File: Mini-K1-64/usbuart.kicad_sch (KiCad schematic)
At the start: 12 parts, among them P1 USB_C_Plug_USB2.0, U1 CH343G, U3 AMS1117-3.3

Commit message: Format PCB
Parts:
- renumbered C8 to C1, C12 to C10, C9 to C7, JP3 to JP2, JP2 to JP3, R9 to R10, R10 to R12
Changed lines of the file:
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@@
 		(dnp no)
 		(fields_autoplaced yes)
-		(property "Reference" "JP2"
+		(property "Reference" "JP3"
 			(at 113.03 135.8901 90)
 			(effects
@@
 			(project "Mini-K1-64"
 				(path "/1a7e0d91-a6c0-4b42-a7c6-42574ab26c7c/391bf1b4-7921-4efb-b6a2-50abc6bbaaa6"
-					(reference "JP2")
+					(reference "JP3")
 					(unit 1)
 				)
@@
 		(dnp no)
 		(fields_autoplaced yes)
-		(property "Reference" "C8"
+		(property "Reference" "C1"
 			(at 180.34 123.1899 0)
 			(effects
@@
 			(project "Mini-K1-64"
 				(path "/1a7e0d91-a6c0-4b42-a7c6-42574ab26c7c/391bf1b4-7921-4efb-b6a2-50abc6bbaaa6"
-					(reference "C8")
+					(reference "C1")
 					(unit 1)
 				)
@@
 		(on_board yes)
 		(dnp yes)
-		(property "Reference" "JP3"
+		(property "Reference" "JP2"
 			(at 100.33 135.8901 90)
 			(effects
@@
 			(project "Mini-K1-64"
 				(path "/1a7e0d91-a6c0-4b42-a7c6-42574ab26c7c/391bf1b4-7921-4efb-b6a2-50abc6bbaaa6"
-					(reference "JP3")
+					(reference "JP2")
 					(unit 1)
 				)
@@
 		(dnp no)
 		(fields_autoplaced yes)
-		(property "Reference" "R9"
+		(property "Reference" "R10"
 			(at 171.45 111.7599 0)
 			(effects
@@
 			(project "Mini-K1-64"
 				(path "/1a7e0d91-a6c0-4b42-a7c6-42574ab26c7c/391bf1b4-7921-4efb-b6a2-50abc6bbaaa6"
-					(reference "R9")
+					(reference "R10")
 					(unit 1)
 				)
@@
 		(dnp no)
 		(fields_autoplaced yes)
-		(property "Reference" "R10"
+		(property "Reference" "R12"
 			(at 125.73 111.7599 0)
 			(effects
@@
 			(project "Mini-K1-64"
 				(path "/1a7e0d91-a6c0-4b42-a7c6-42574ab26c7c/391bf1b4-7921-4efb-b6a2-50abc6bbaaa6"
-					(reference "R10")
+					(reference "R12")
 					(unit 1)
 				)
@@
 		(dnp no)
 		(fields_autoplaced yes)
-		(property "Reference" "C9"
+		(property "Reference" "C7"
 			(at 167.64 123.1899 0)
 			(effects
@@
 			(project "Mini-K1-64"
 				(path "/1a7e0d91-a6c0-4b42-a7c6-42574ab26c7c/391bf1b4-7921-4efb-b6a2-50abc6bbaaa6"
-					(reference "C9")
+					(reference "C7")
 					(unit 1)
 				)
@@
 		(on_board yes)
 		(dnp no)
-		(property "Reference" "C12"
+		(property "Reference" "C10"
 			(at 135.89 123.1899 0)
 			(effects
@@
 			(project "Mini-K1-64"
 				(path "/1a7e0d91-a6c0-4b42-a7c6-42574ab26c7c/391bf1b4-7921-4efb-b6a2-50abc6bbaaa6"
-					(reference "C12")
-					(unit 1)
-				)
+					(reference "C10")
+					(unit 1)
+				)

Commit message: Step Update
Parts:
- removed P1: USB_C_Plug_USB2.0, Connector_USB:USB_C_Receptacle_GCT_USB4105-xx-A_16P_TopMnt_Horizontal, symbol Connector:USB_C_Plug_USB2.0
- removed U1: CH343G, Package_SO:SOIC-16_3.9x9.9mm_P1.27mm, symbol Interface_USB:CH343G
- added J6: USB_C_Receptacle_USB2.0_14P, Connector_USB:USB_C_Receptacle_GCT_USB4105-xx-A_16P_TopMnt_Horizontal, symbol Connector:USB_C_Receptacle_USB2.0_14P
- added R16: 5.1K, Resistor_SMD:R_0805_2012Metric, symbol Device:R
- added U1: CH340N, Package_SO:SOP-8_3.9x4.9mm_P1.27mm, symbol Interface_USB:CH340N
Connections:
- net OGND: now also J6.A1 (GND), J6.A12 (GND), J6.B1 (GND), J6.B12 (GND), J6.S1 (SHIELD), R16.2, U1.3 (GND)
- net UART_RX: now also U1.7 (RXD)
- net UART_TX: now also U1.6 (TXD)
- net UD+: now also J6.A6 (D+), J6.B6 (D+), U1.1 (UD+)
- net UD-: now also J6.A7 (D-), J6.B7 (D-), U1.2 (UD-)
- net VBUS: now also J6.A4 (VBUS), J6.A9 (VBUS), J6.B4 (VBUS), J6.B9 (VBUS), U1.5 (VCC)
- net at C1.1: now also U1.8 (V3)
- net at R10.1: now also J6.A5 (CC1)
- new net: J6.B5 (CC2), R16.1
- no-connect marks 8 -> 1
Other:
- moved on the sheet: C7, R10, U3

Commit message: Rev0
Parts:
- renumbered J6 to J1, R16 to R10, R10 to R11, R12 to R13
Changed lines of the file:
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@@
 		(dnp no)
 		(fields_autoplaced yes)
-		(property "Reference" "J6"
+		(property "Reference" "J1"
 			(at 102.87 82.55 0)
 			(effects
@@
 			(project "Mini-K1-64"
 				(path "/1a7e0d91-a6c0-4b42-a7c6-42574ab26c7c/391bf1b4-7921-4efb-b6a2-50abc6bbaaa6"
-					(reference "J6")
+					(reference "J1")
 					(unit 1)
 				)
@@
 		(dnp no)
 		(fields_autoplaced yes)
-		(property "Reference" "R10"
+		(property "Reference" "R11"
 			(at 170.18 111.7599 0)
 			(effects
@@
 			(project "Mini-K1-64"
 				(path "/1a7e0d91-a6c0-4b42-a7c6-42574ab26c7c/391bf1b4-7921-4efb-b6a2-50abc6bbaaa6"
-					(reference "R10")
+					(reference "R11")
 					(unit 1)
 				)
@@
 		(dnp no)
 		(fields_autoplaced yes)
-		(property "Reference" "R12"
+		(property "Reference" "R13"
 			(at 125.73 111.7599 0)
 			(effects
@@
 			(project "Mini-K1-64"
 				(path "/1a7e0d91-a6c0-4b42-a7c6-42574ab26c7c/391bf1b4-7921-4efb-b6a2-50abc6bbaaa6"
-					(reference "R12")
+					(reference "R13")
 					(unit 1)
 				)
@@
 		(dnp no)
 		(fields_autoplaced yes)
-		(property "Reference" "R16"
+		(property "Reference" "R10"
 			(at 162.56 111.7599 0)
 			(effects
@@
 			(project "Mini-K1-64"
 				(path "/1a7e0d91-a6c0-4b42-a7c6-42574ab26c7c/391bf1b4-7921-4efb-b6a2-50abc6bbaaa6"
-					(reference "R16")
-					(unit 1)
-				)
+					(reference "R10")
+					(unit 1)
+				)

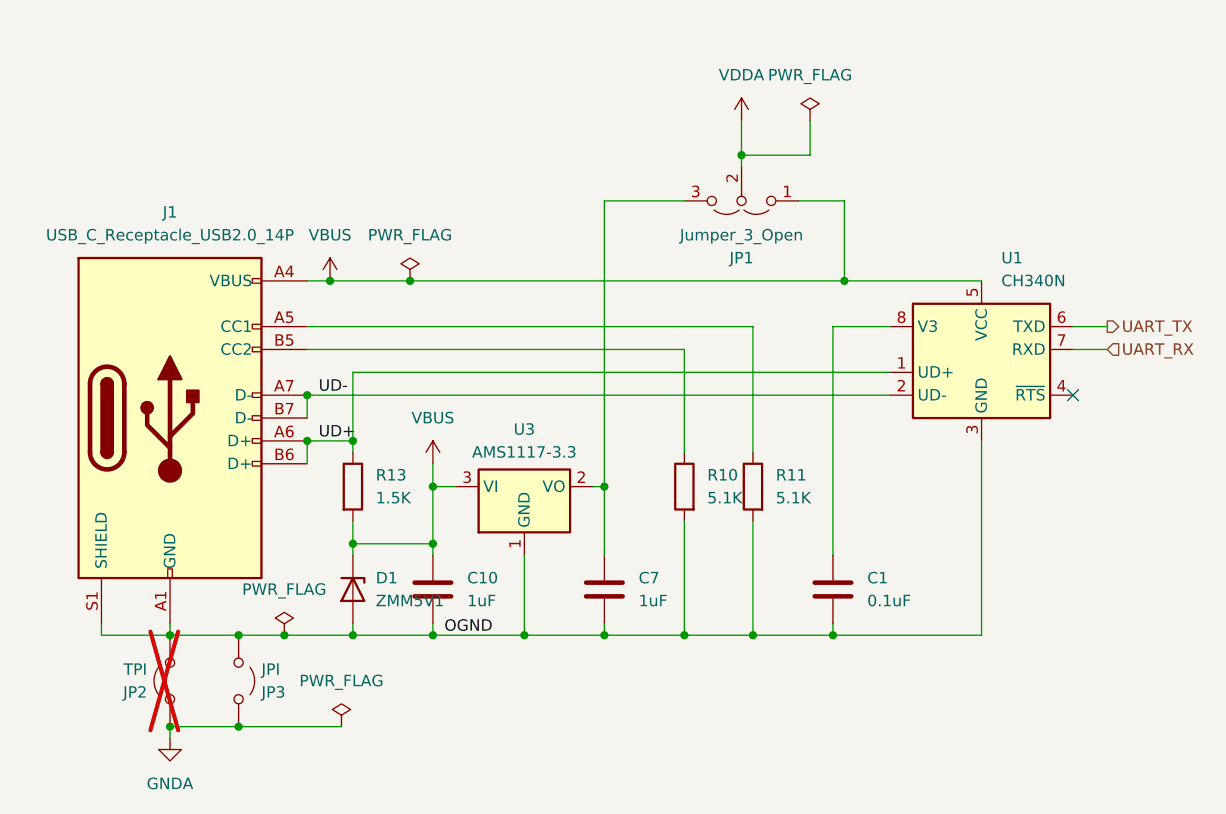
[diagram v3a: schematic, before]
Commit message: Update Debug Connector
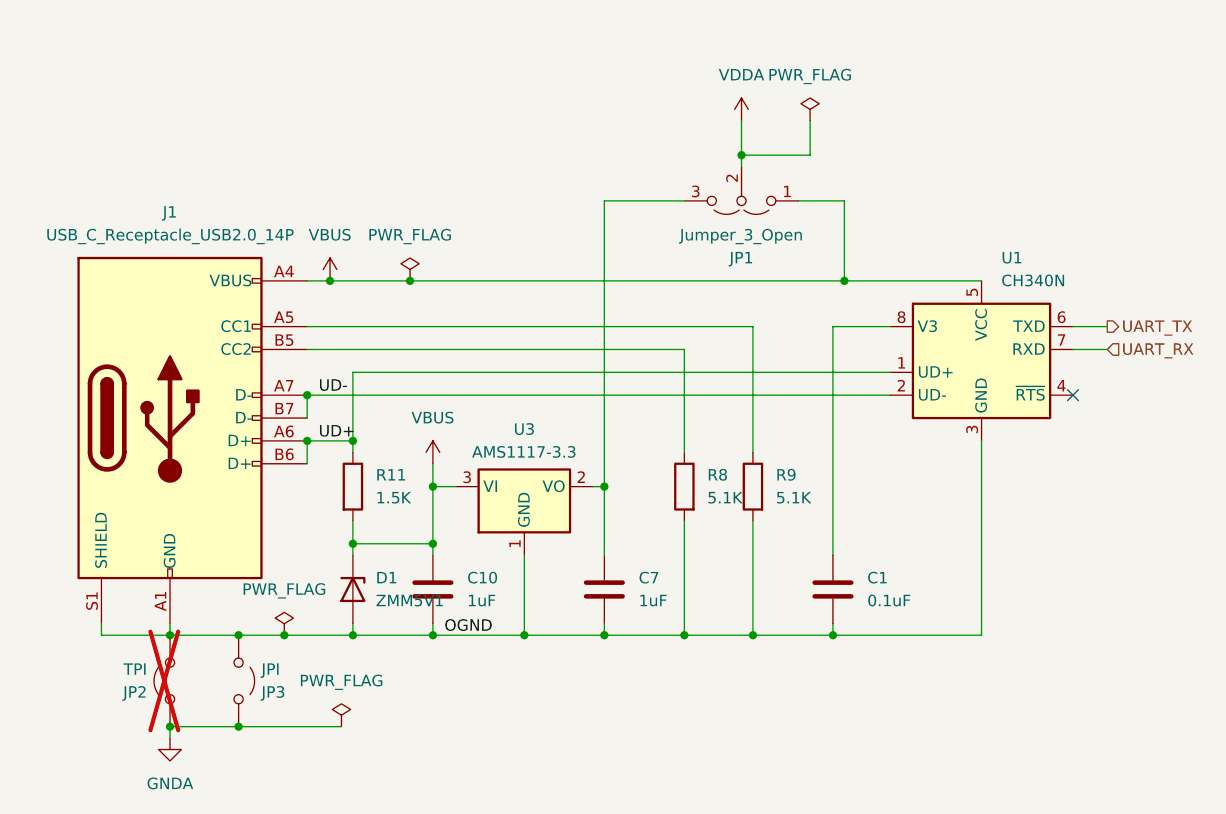
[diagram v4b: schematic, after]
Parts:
- renumbered R13 to R11, R10 to R8, R11 to R9
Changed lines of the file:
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@@
 		(dnp no)
 		(fields_autoplaced yes)
-		(property "Reference" "R11"
+		(property "Reference" "R9"
 			(at 170.18 111.7599 0)
 			(effects
@@
 			(project "Mini-K1-64"
 				(path "/1a7e0d91-a6c0-4b42-a7c6-42574ab26c7c/391bf1b4-7921-4efb-b6a2-50abc6bbaaa6"
-					(reference "R11")
+					(reference "R9")
 					(unit 1)
 				)
@@
 		(dnp no)
 		(fields_autoplaced yes)
-		(property "Reference" "R13"
+		(property "Reference" "R11"
 			(at 125.73 111.7599 0)
 			(effects
@@
 			(project "Mini-K1-64"
 				(path "/1a7e0d91-a6c0-4b42-a7c6-42574ab26c7c/391bf1b4-7921-4efb-b6a2-50abc6bbaaa6"
-					(reference "R13")
+					(reference "R11")
 					(unit 1)
 				)
@@
 		(dnp no)
 		(fields_autoplaced yes)
-		(property "Reference" "R10"
+		(property "Reference" "R8"
 			(at 162.56 111.7599 0)
 			(effects
@@
 			(project "Mini-K1-64"
 				(path "/1a7e0d91-a6c0-4b42-a7c6-42574ab26c7c/391bf1b4-7921-4efb-b6a2-50abc6bbaaa6"
-					(reference "R10")
-					(unit 1)
-				)
+					(reference "R8")
+					(unit 1)
+				)

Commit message: Update to Kicad 9
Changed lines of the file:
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@@
 (kicad_sch
-	(version 20231120)
+	(version 20250114)
 	(generator "eeschema")
-	(generator_version "8.0")
+	(generator_version "9.0")
 	(paper "A4")
 	(title_block
@@
 	(label "UD+"
 		(at 119.38 107.95 0)
-		(fields_autoplaced yes)
 		(effects
 			(font
@@
 	(label "UD-"
 		(at 119.38 102.87 0)
-		(fields_autoplaced yes)
 		(effects
 			(font
@@
 	(label "OGND"
 		(at 133.35 129.54 0)
-		(fields_autoplaced yes)
 		(effects
 			(font
@@
 		(shape input)
 		(at 207.01 97.79 0)
-		(fields_autoplaced yes)
 		(effects
 			(font
@@
 		(shape output)
 		(at 207.01 95.25 0)
-		(fields_autoplaced yes)
 		(effects
 			(font
